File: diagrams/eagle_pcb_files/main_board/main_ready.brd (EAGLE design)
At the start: 67.8 x 31.5 mm, 31 parts

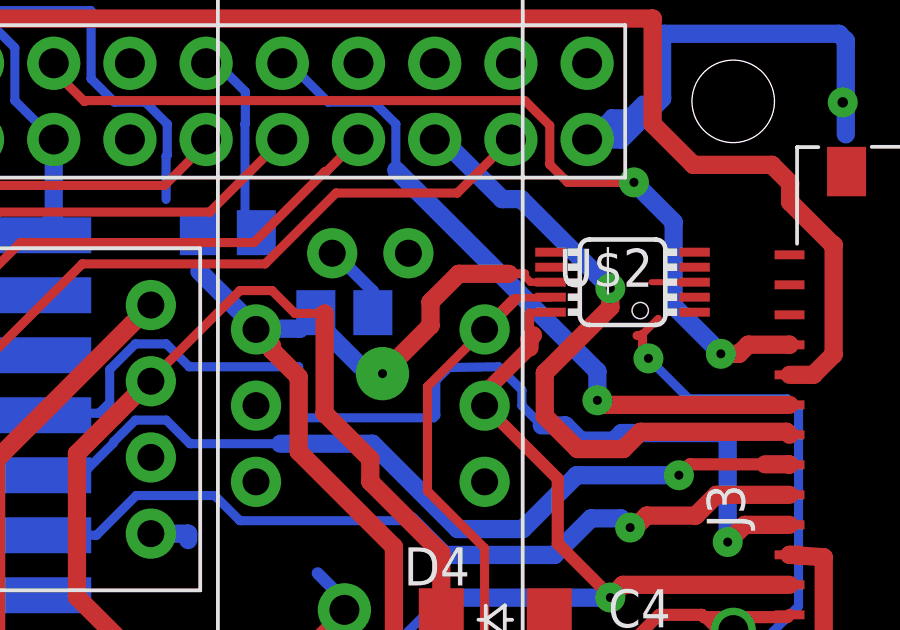
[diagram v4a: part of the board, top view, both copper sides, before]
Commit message: remove adc from main board
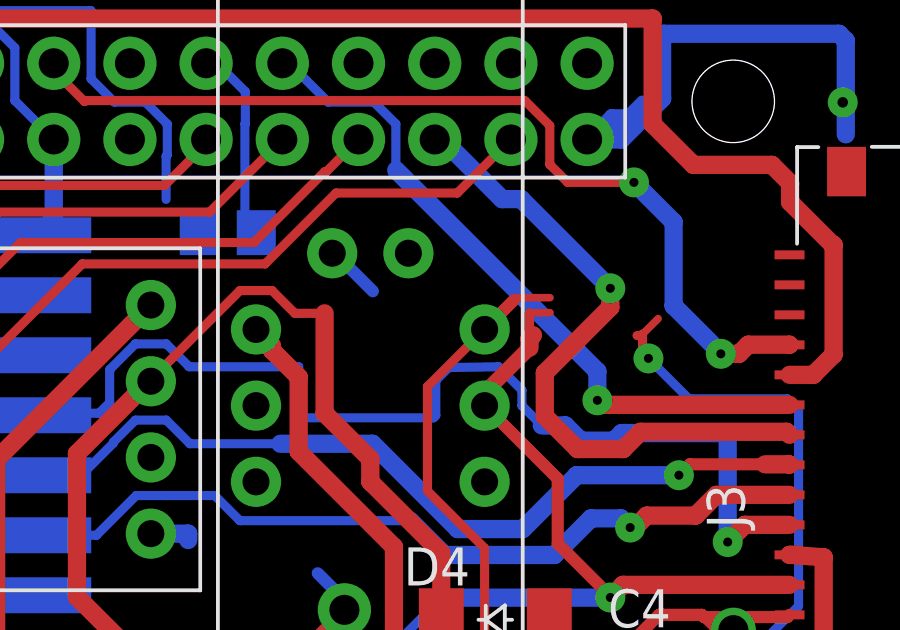
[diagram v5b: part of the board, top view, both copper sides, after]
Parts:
- removed C5: 100nF, rcl:C0805
- removed U$2: ADS1015IDGT, bt_adc:MSOP10_0.5
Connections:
- net 3.3V: no longer C5.2, U$2.8
- net A0: no longer U$2.4
- net A1: no longer U$2.5
- net GND: no longer C5.1, U$2.3
- net SCL: no longer U$2.10
- net SDA: no longer U$2.9
- net VIN1: now also J2.9
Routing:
- net 3.3V: track 131.8 -> 116.0 mm, vias 3 -> 2
- net GND: track 171.3 -> 169.2 mm
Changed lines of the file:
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@@
 <attribute name="VALUE" x="111.9378" y="33.0962" size="1.27" layer="27"/>
-</element>
-<element name="C5" library="rcl" library_urn="urn:adsk.eagle:library:334" package="C0805" package3d_urn="urn:adsk.eagle:package:23617/2" value="100nF" x="103.1494" y="47.3964" smashed="yes" rot="MR0">
-<attribute name="NAME" x="102.4636" y="48.9458" size="1.27" layer="26" rot="MR0"/>
-<attribute name="SPICEPREFIX" value="C" x="85.3694" y="-50.3936" size="1.778" layer="28" rot="MR0" display="off"/>
-<attribute name="VALUE" x="104.4194" y="44.8564" size="1.27" layer="28" rot="MR0"/>
 </element>
 <element name="C6" library="rcl" library_urn="urn:adsk.eagle:library:334" package="C0805" package3d_urn="urn:adsk.eagle:package:23617/2" value="100nF" x="99.2632" y="50.0634" smashed="yes" rot="MR180">
@@
 <attribute name="TP_SIGNAL_NAME" value="" x="97.028" y="28.7782" size="1" layer="37"/>
 <attribute name="VALUE" x="96.7232" y="30.5054" size="0.0254" layer="27"/>
-</element>
-<element name="U$2" library="bt_adc" package="MSOP10_0.5" value="ADS1015IDGT" x="112.4204" y="48.4124" smashed="yes" rot="R90">
-<attribute name="NAME" x="113.4364" y="49.53" size="1.27" layer="25" ratio="10" rot="R180"/>
-<attribute name="VALUE" x="114.9096" y="50.673" size="1.27" layer="27" ratio="10" rot="R180"/>
 </element>
 <element name="U$3" library="SparFun-FuelGauge" package="BREAKBOARD" value="POLOLU_FUEL_GAUGEBREAKBOARD" x="62.9412" y="38.1254" smashed="yes"/>
@@
 <contactref element="C4" pad="1"/>
 <contactref element="J3" pad="2"/>
-<contactref element="C5" pad="1"/>
 <contactref element="GND" pad="TP"/>
 <contactref element="RAO1" pad="9"/>
@@
 <wire x1="111.8186" y1="53.17" x2="111.24" y2="53.17" width="0.4064" layer="16"/>
 <wire x1="112.045" y1="53.975" x2="112.6236" y2="53.975" width="0.4064" layer="16"/>
-<wire x1="104.0994" y1="47.3964" x2="104.0994" y2="48.11049375" width="0.4064" layer="16"/>
 <wire x1="104.0994" y1="48.11049375" x2="102.83229375" y2="49.3776" width="0.4064" layer="16"/>
 <wire x1="102.83229375" y1="49.3776" x2="102.743" y2="49.3776" width="0.4064" layer="16"/>
@@
 <via x="119.761" y="54.4068" extent="1-16" drill="0.35" diameter="1"/>
 <wire x1="119.634" y1="56.6928" x2="119.8626" y2="56.4642" width="0.6096" layer="16"/>
-<contactref element="U$2" pad="3"/>
-<wire x1="114.8204" y1="48.4124" x2="113.3856" y2="48.4124" width="0.2032" layer="1"/>
 <contactref element="RAO3" pad="GND"/>
 <contactref element="C10" pad="-"/>
@@
 <contactref element="C7" pad="1"/>
 <contactref element="SJ1" pad="2"/>
+<contactref element="J2" pad="9"/>
+<wire x1="66.4684" y1="36.83" x2="87.3708" y2="32.3038" width="0" layer="19" extent="1-1"/>
 <wire x1="63.3476" y1="41.1124" x2="66.4684" y2="36.83" width="0" layer="19" extent="1-16"/>
 <wire x1="59.1312" y1="44.4754" x2="63.3476" y2="41.1124" width="0" layer="19" extent="16-16"/>
@@
 <contactref element="RAO2" pad="17"/>
 <contactref element="C2" pad="1"/>
-<contactref element="U$2" pad="8"/>
-<contactref element="C5" pad="2"/>
 <wire x1="73.787" y1="39.8628" x2="75.7276" y2="39.8628" width="0.6096" layer="16"/>
 <wire x1="75.7276" y1="39.8628" x2="75.7428" y2="39.878" width="0.6096" layer="16"/>
@@
 <wire x1="60.3961" y1="48.9509" x2="59.1312" y2="47.686" width="0.6096" layer="1"/>
 <wire x1="59.1312" y1="47.686" x2="59.1312" y2="47.4726" width="0.6096" layer="1"/>
-<wire x1="101.666" y1="46.863" x2="100.2284" y2="46.863" width="0.6096" layer="16"/>
-<wire x1="101.666" y1="46.863" x2="102.1994" y2="47.3964" width="0.6096" layer="16"/>
-<wire x1="102.1994" y1="47.3964" x2="102.1994" y2="47.1018" width="0.6096" layer="16"/>
-<wire x1="102.1994" y1="47.1018" x2="103.6574" y2="45.6438" width="0.6096" layer="16"/>
-<wire x1="103.6574" y1="45.6438" x2="104.14" y2="45.6438" width="0.6096" layer="16"/>
-<wire x1="104.14" y1="45.6438" x2="104.4194" y2="45.3644" width="0.6096" layer="16"/>
-<via x="104.4194" y="45.3644" extent="1-16" drill="0.3" diameter="1.778" shape="octagon"/>
-<wire x1="104.4194" y1="45.3644" x2="106.0196" y2="46.9646" width="0.6096" layer="1"/>
-<wire x1="106.0196" y1="46.9646" x2="106.0196" y2="47.752" width="0.6096" layer="1"/>
-<wire x1="106.0196" y1="47.752" x2="106.9594" y2="48.6918" width="0.6096" layer="1"/>
-<wire x1="106.9594" y1="48.6918" x2="108.6358" y2="48.6918" width="0.6096" layer="1"/>
-<wire x1="108.6358" y1="48.6918" x2="109.14995" y2="48.6918" width="0.3048" layer="1"/>
 <wire x1="82.52013125" y1="53.17" x2="83.3" y2="53.17" width="0.4064" layer="1"/>
 <wire x1="60.3961" y1="48.9509" x2="60.3961" y2="48.7375" width="0.4064" layer="1"/>
@@
 <wire x1="73.5584" y1="34.1528" x2="73.9334" y2="33.7778" width="0.6096" layer="1"/>
 <wire x1="73.9334" y1="33.7778" x2="77.5758" y2="33.7778" width="0.6096" layer="1"/>
-<wire x1="98.3132" y1="48.7782" x2="100.2284" y2="46.863" width="0.6096" layer="16"/>
 <wire x1="97.2058" y1="51.1708" x2="97.2058" y2="52.61566875" width="0.3048" layer="16"/>
 <wire x1="97.2446" y1="52.65446875" x2="97.2058" y2="52.61566875" width="0.3048" layer="16"/>
@@
 <wire x1="97.2446" y1="53.68553125" x2="97.2446" y2="52.65446875" width="0.3048" layer="16"/>
 <wire x1="85.83246875" y1="57.4626" x2="94.7046" y2="57.4626" width="0.3048" layer="16"/>
-<wire x1="109.14995" y1="48.6918" x2="109.1548" y2="48.68695" width="0.3048" layer="1"/>
-<wire x1="109.1548" y1="48.68695" x2="109.1548" y2="48.61510625" width="0.3048" layer="1"/>
-<wire x1="109.1548" y1="48.61510625" x2="109.35750625" y2="48.4124" width="0.254" layer="1"/>
-<wire x1="109.35750625" y1="48.4124" x2="110.0204" y2="48.4124" width="0.254" layer="1"/>
 <wire x1="62.98" y1="53.582" x2="62.98" y2="53.213" width="0.3048" layer="1"/>
 <wire x1="62.98" y1="53.213" x2="62.98" y2="53.17" width="0.3048" layer="1"/>
@@
 <wire x1="73.0098" y1="39.8628" x2="73.787" y2="39.8628" width="0.6096" layer="16"/>
 <wire x1="71.9074" y1="38.7604" x2="73.0098" y2="39.8628" width="0.6096" layer="16"/>
-<wire x1="100.7364" y1="46.3042" x2="100.2284" y2="46.863" width="0" layer="19" extent="1-16"/>
-<wire x1="97.2058" y1="51.1708" x2="98.3132" y2="48.7782" width="0" layer="19" extent="16-16"/>
+<wire x1="97.2058" y1="51.1708" x2="100.7364" y2="46.3042" width="0" layer="19" extent="1-16"/>
 <wire x1="64.6938" y1="39.7662" x2="59.1312" y2="47.4726" width="0" layer="19" extent="1-16"/>
 </signal>
@@
 <contactref element="U$9" pad="SCL"/>
 <contactref element="J3" pad="3"/>
-<contactref element="U$2" pad="10"/>
 <wire x1="68.06" y1="53.17" x2="68.06" y2="45.4406" width="0.3048" layer="1"/>
 <wire x1="68.06" y1="45.4406" x2="68.06" y2="43.2442" width="0.3048" layer="1"/>
@@
 <wire x1="112.014" y1="37.9476" x2="112.014" y2="37.902" width="0.4064" layer="1"/>
 <wire x1="109.3216" y1="47.3964" x2="110.0044" y2="47.3964" width="0.254" layer="1"/>
-<wire x1="110.0044" y1="47.3964" x2="110.0204" y2="47.4124" width="0.254" layer="1"/>
 <wire x1="68.06" y1="45.4406" x2="76.35121875" y2="45.4406" width="0.3048" layer="1"/>
 <wire x1="76.35121875" y1="45.4406" x2="76.42741875" y2="45.3644" width="0.3048" layer="1"/>
@@
 <contactref element="U$9" pad="SDA"/>
 <contactref element="J3" pad="4"/>
-<contactref element="U$2" pad="9"/>
 <wire x1="65.52" y1="53.17" x2="66.7512" y2="51.9388" width="0.6096" layer="1"/>
 <wire x1="66.7512" y1="51.9388" x2="66.7512" y2="44.4754" width="0.6096" layer="1"/>
@@
 <wire x1="107.823" y1="39.5478" x2="107.823" y2="35.4838" width="0.3048" layer="1"/>
 <wire x1="105.918" y1="41.4528" x2="107.823" y2="39.5478" width="0.3048" layer="1"/>
-<wire x1="110.0204" y1="47.9124" x2="110.003" y2="47.895" width="0.254" layer="1"/>
 <wire x1="108.8804" y1="47.895" x2="108.7882" y2="47.8028" width="0.254" layer="1"/>
 <wire x1="110.003" y1="47.895" x2="108.8804" y2="47.895" width="0.254" layer="1"/>
@@
 </signal>
 <signal name="A0">
-<contactref element="U$2" pad="4"/>
 <contactref element="J3" pad="12"/>
-<wire x1="117.988" y1="47.3244" x2="114.8204" y2="48.9124" width="0" layer="19" extent="1-1"/>
 </signal>
 <signal name="A1">
-<contactref element="U$2" pad="5"/>
 <contactref element="J3" pad="13"/>
-<wire x1="114.8204" y1="49.4124" x2="117.988" y2="48.3244" width="0" layer="19" extent="1-1"/>
 </signal>
 <signal name="BUZ">

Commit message: main board ready for production
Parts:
- moved SJ2 111.3 mm to (114.6, 49.2)
- moved C13 87.9 mm to (101.2, 37.8), turned to 270 degrees
- moved C12 83.9 mm to (99.0, 38.1), turned to 270 degrees
- moved C10 60.5 mm to (74.3, 40.3)
- moved SJ1 57.5 mm to (56.7, 36.8), turned to 90 degrees
- moved FUSE1 7.43 mm to (72.5, 29.1), turned to 0 degrees
- moved C7 6.64 mm to (56.8, 43.1), turned to 270 degrees
- moved D1 4.57 mm to (69.2, 37.0), turned to 270 degrees
- moved BAT1 0.10 mm to (64.8, 34.0), turned to 180 degrees
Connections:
- net GND: no longer RAO2.9
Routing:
- net VIN1: track 0.00 -> 54.9 mm, vias 0 -> 3
- net VIN2: track 0.00 -> 49.6 mm, vias 0 -> 3
- net GND: track 169.2 -> 126.7 mm, vias 5 -> 6
- net BIN2: track 0.00 -> 26.1 mm
- net SHDN1: track 41.0 -> 22.6 mm
- net SDA: track 116.0 -> 99.5 mm, vias 2 -> 3
- net B: track 37.4 -> 22.8 mm, vias 1 -> 0
- net SCL: track 90.7 -> 105.0 mm, vias 2 -> 3
- net BIN1: track 8.12 -> 21.5 mm
- net 3.3V: track 116.0 -> 127.7 mm, vias 2 -> 1
- net A: track 0.00 -> 9.22 mm
- net VOUT1: track 8.68 -> 17.7 mm
- net VOUT2: track 5.99 -> 14.9 mm
- net 5V: track 0.00 -> 2.54 mm
- net SHDN2: track 18.6 -> 20.8 mm
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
